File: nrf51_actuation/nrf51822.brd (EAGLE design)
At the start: 40 x 27.8 mm, 22 parts, among them T1 MMUN2238

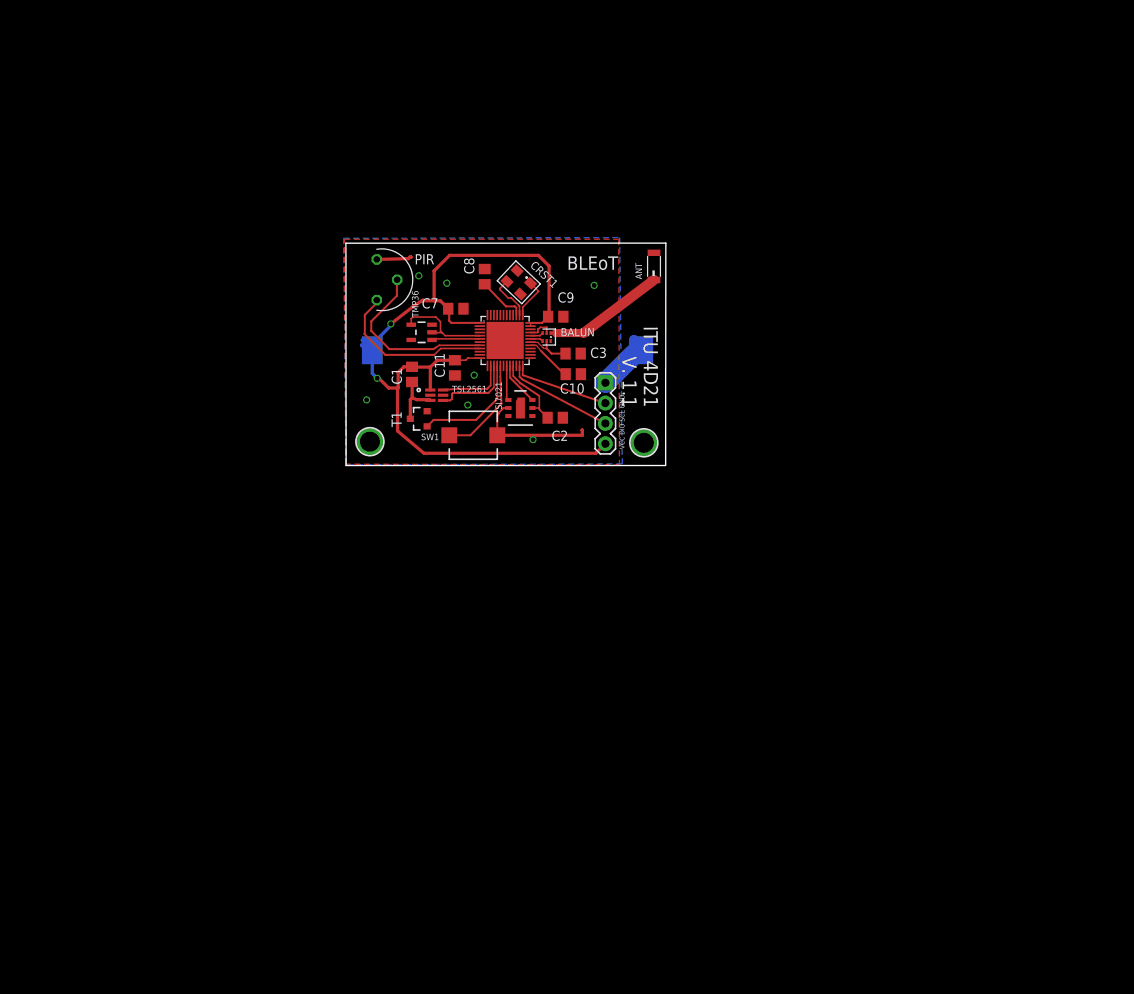
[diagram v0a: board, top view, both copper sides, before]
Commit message: Sensor board should be 100% done... Waiting for boards from slow china :0)
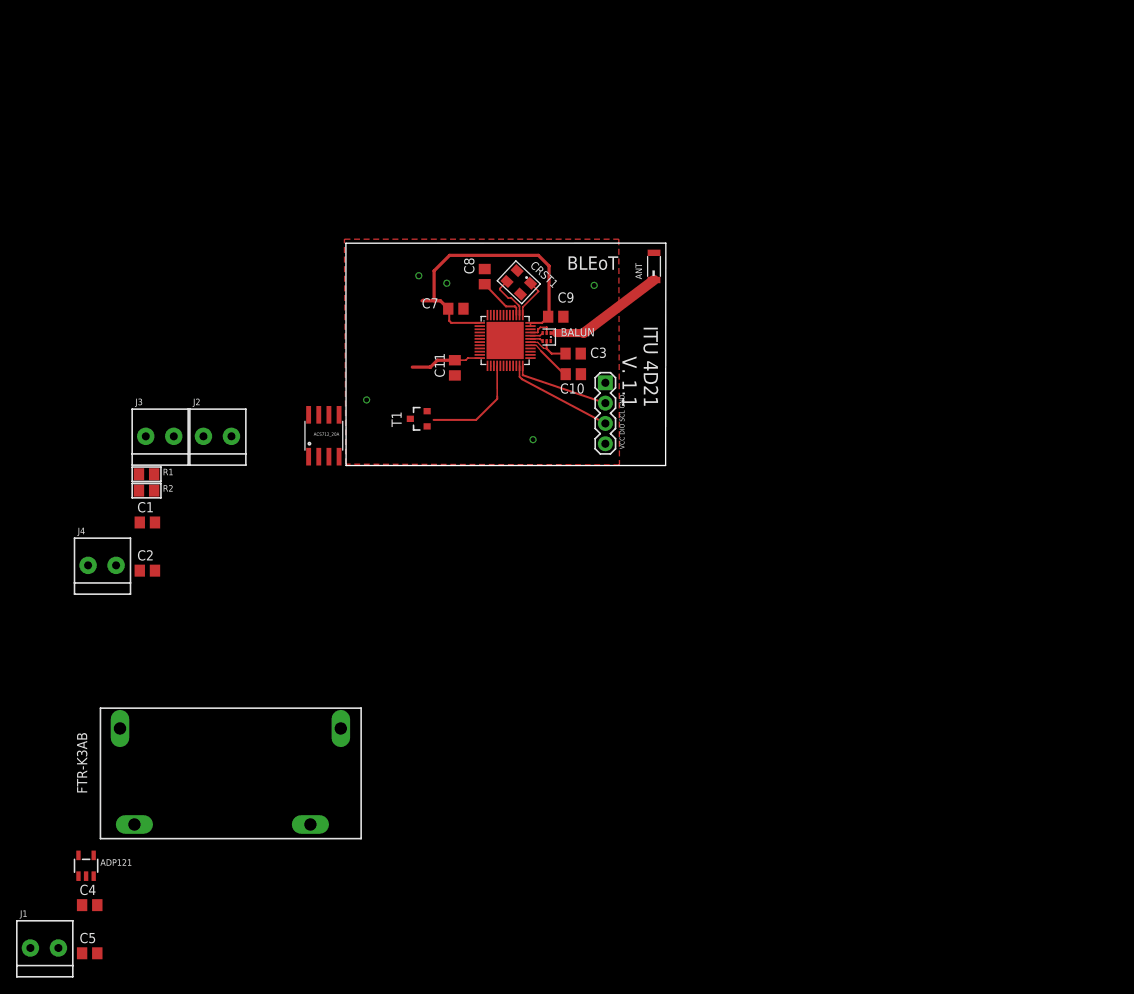
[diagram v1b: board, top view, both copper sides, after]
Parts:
- removed CR2450: 3.3V, NordicSemi:CR2450
- removed PIR: EKMB1303112, NordicSemi:TO5
- removed SI7021: SI7021SMD, NordicSemi:SI7021
- removed SW1: (no value), microbuilder:PUSHBUTTON_SMD_SJ
- removed TMP36: TMP36_SOT23_5, NordicSemi:SOT23-5
- removed TSL2561: LIGHT_TSL2561, microbuilder:TSL2561_FN
- removed U$6, U$7: MOUNTINGHOLE2.5, microbuilder:MOUNTINGHOLE_2.5_PLATED
- added ACS712_20A: ACS712, SparkFun-AnalogIC:SO08
- added ADP121: (no value), microbuilder:SOT23-5
- added C4, C5: 10uF, rcl:C0805
- added FTR-K3AB: FTR-K3AB, NordicSemi:FTR-K1C
- added J1, J2, J3, J4: (no value), microbuilder:TERMBLOCK_1X2-3.5MM
- added R1, R2: (no value), microbuilder:0805
- C1: value 100nF -> 1nF
- moved C2 54.4 mm to (-23.3, -11.3)
- moved C1 37.9 mm to (-23.3, -5.31), turned to 0 degrees
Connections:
- removed net GIOP3: SW1.P$2, U$4.17
- new net 5.0V: ACS712_20A.8, ADP121.1, ADP121.3, C2.1, C5.1, FTR-K3AB.1, J3.1
- new net N$11: ACS712_20A.6, C1.1
- new net N$15: ACS712_20A.7, R1.1
- new net ROUT1: ACS712_20A.1, ACS712_20A.2, FTR-K3AB.4, J2.1, J4.1
- new net ROUT2: ACS712_20A.3, ACS712_20A.4, FTR-K3AB.3, J2.2, J4.2
- new net TERMO1: J1.1
- new net TERMO2: J1.2
- net AIN0/XL2: now also R1.2, R2.1
- net AIN2: no longer TMP36.2, TMP36.4
- net AIN3: no longer TMP36.1
- net AIN5: no longer PIR.2
- net AIN6: no longer PIR.1
- net GIOP0: no longer TSL2561.DATA
- net GIOP1: no longer TSL2561.CLK
- net GIOP5: no longer SI7021.1
- net GIOP6: no longer SI7021.6
- net GIOP7: no longer C2.1, SI7021.5
- net GND: now also ACS712_20A.5, ADP121.2, C1.2, C4.2, C5.2, J3.2, R2.2; no longer CR2450.NEG, PIR.3, SI7021.2, SW1.P$1, TMP36.5
- net N$7: now also FTR-K3AB.2; no longer C1.1, TSL2561.VSS
- net VDD: now also ADP121.5, C4.1; no longer C1.2, CR2450.POS, TSL2561.VDD
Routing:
- net VDD: track 108.3 -> 49.5 mm, vias 2 -> 0
- net GND: track 31.9 -> 3.31 mm, vias 7 -> 5
- net AIN5: track 22.4 -> 0.00 mm
- net AIN6: track 20.7 -> 0.00 mm
- net GIOP3: track 12.9 -> 0.00 mm
- net AIN2: track 12.4 -> 0.01 mm
- net GIOP1: track 10.1 -> 0.00 mm
- net GIOP7: track 9.43 -> 0.00 mm
- net GIOP0: track 8.61 -> 0.04 mm
- net N$7: track 7.19 -> 0.00 mm
- net AIN3: track 6.02 -> 0.00 mm
- net GIOP6: track 5.43 -> 0.00 mm
- net GIOP5: track 4.36 -> 0.00 mm
- net GIOP2: track 14.4 -> 13.2 mm
- removed copper zone on layer 16, net GND

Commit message: Done with routing.. should be more or less done
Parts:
- removed J3: (no value), microbuilder:TERMBLOCK_1X2-3.5MM
- added AD8495: AD8495, NordicSemi:MSOP-8
- added C12: 100nF, rcl:C0805
- added C13, C14: 12pF, rcl:C0805
- added C6: 10nF, rcl:C0805
- added FB1, FB2: (no value), microbuilder:0805
- added IRM-05-5: IRM05-5V, NordicSemi:IRM05
- added U$1, U$13, U$14, U$7: MOUNTINGHOLE2.5, microbuilder:MOUNTINGHOLE_2.5_PLATED
- moved FTR-K3AB 124.4 mm to (79.7, 45.7)
- moved J4 123.7 mm to (93.8, 3.89), turned to 180 degrees
- moved C5 111.2 mm to (48.6, 18.9), turned to 270 degrees
- moved C4 102.3 mm to (41.5, 19.5), turned to 90 degrees
- moved ADP121 101.8 mm to (45.0, 19.5), turned to 90 degrees
- moved J1 81.7 mm to (4.34, 12.4), turned to 90 degrees
- moved C2 71.9 mm to (24.4, 42.4), turned to 270 degrees
- moved C1 65.0 mm to (19.3, 43.7), turned to 180 degrees
- moved R1 55.7 mm to (22.5, 32.2), turned to 270 degrees
- moved R2 52.8 mm to (22.6, 24.6), turned to 211.8 degrees
- moved J2 51.1 mm to (4.36, 52.9), turned to 90 degrees
- moved ACS712_20A 49.0 mm to (21.9, 48.7), turned to 180 degrees
- moved T1 39.7 mm to (50.3, 7.29), turned to 270 degrees
- moved ANT 25.8 mm to (46.6, 1.81), turned to 0 degrees
- moved C8 9.69 mm to (27.2, 20.5), turned to 0 degrees
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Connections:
- removed net ROUT1: ACS712_20A.1, ACS712_20A.2, FTR-K3AB.4, J2.1, J4.1
- removed net ROUT2: ACS712_20A.3, ACS712_20A.4, FTR-K3AB.3, J2.2, J4.2
- removed net TERMO1: J1.1
- removed net TERMO2: J1.2
- new net AC/L: ACS712_20A.1, ACS712_20A.2, IRM-05-5.AC/L, J4.1
- new net AC/LOUT: ACS712_20A.3, ACS712_20A.4, J2.2
- new net AC/N: FTR-K3AB.3, IRM-05-5.AC/N, J4.2
- new net AC/NOUT: FTR-K3AB.4, J2.1
- new net GIOP10: U$4.25
- new net GIOP3: U$4.17
- new net N$16: AD8495.1, C6.2, FB2.2
- new net N$17: FB2.1, J1.2
- new net N$8: FB1.1, J1.1
- new net N$9: AD8495.8, C6.1, FB1.2
- net 5.0V: now also AD8495.7, C12.2, IRM-05-5.+V; no longer J3.1
- net AIN4: now also AD8495.5, AD8495.6
- net GND: now also AD8495.2, AD8495.3, C12.1, C13.1, C14.1, IRM-05-5.-V; no longer J3.2
- net N$1: now also C14.2, CRST1.H2, U$4.38; no longer CRST1.H1, U$4.37
- net N$2: now also C13.2, CRST1.H1, U$4.37; no longer CRST1.H2, U$4.38
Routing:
- net 5.0V: track 0.00 -> 152.5 mm, vias 0 -> 2
- net AC/L: track 0.00 -> 98.1 mm, vias 0 -> 1
- net AC/NOUT: track 0.00 -> 63.2 mm
- net N$7: track 0.00 -> 53.8 mm
- net AC/N: track 0.00 -> 50.0 mm
- net VDD: track 49.5 -> 96.4 mm, vias 0 -> 4
- net GND: track 3.31 -> 26.7 mm, vias 5 -> 9
- net AC/LOUT: track 0.00 -> 18.2 mm
- net GIOP2: track 13.2 -> 29.8 mm, vias 0 -> 3
- net AIN0/XL2: track 0.00 -> 16.2 mm
- net N$15: track 0.00 -> 12.9 mm
- net AIN4: track 0.00 -> 8.01 mm
- net N$16: track 0.00 -> 7.39 mm
- net N$9: track 0.00 -> 6.45 mm
- net N$3: track 15.1 -> 21.4 mm
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- added copper zone on layer 16, net GND
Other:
- board size 40 x 27.8 mm -> 97.2 x 56.6 mm
- board text removed: "BLEoT"
- board text removed: "ITU 4D21 V. 1.1"
- board text removed: "VCC DIO SCL GND"

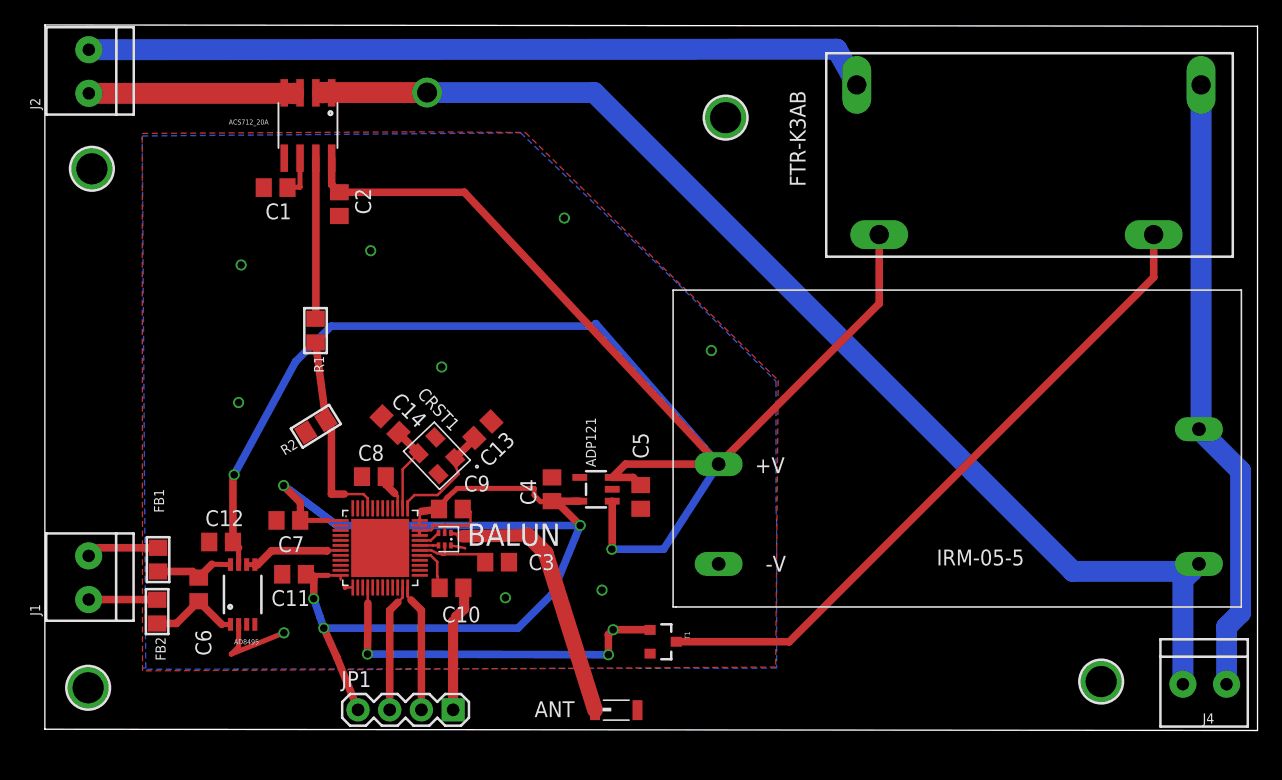
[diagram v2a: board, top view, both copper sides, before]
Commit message: CLEANED AND ADDED COMMENTS / TAGS ACTUATION MADE 45% SMALLER
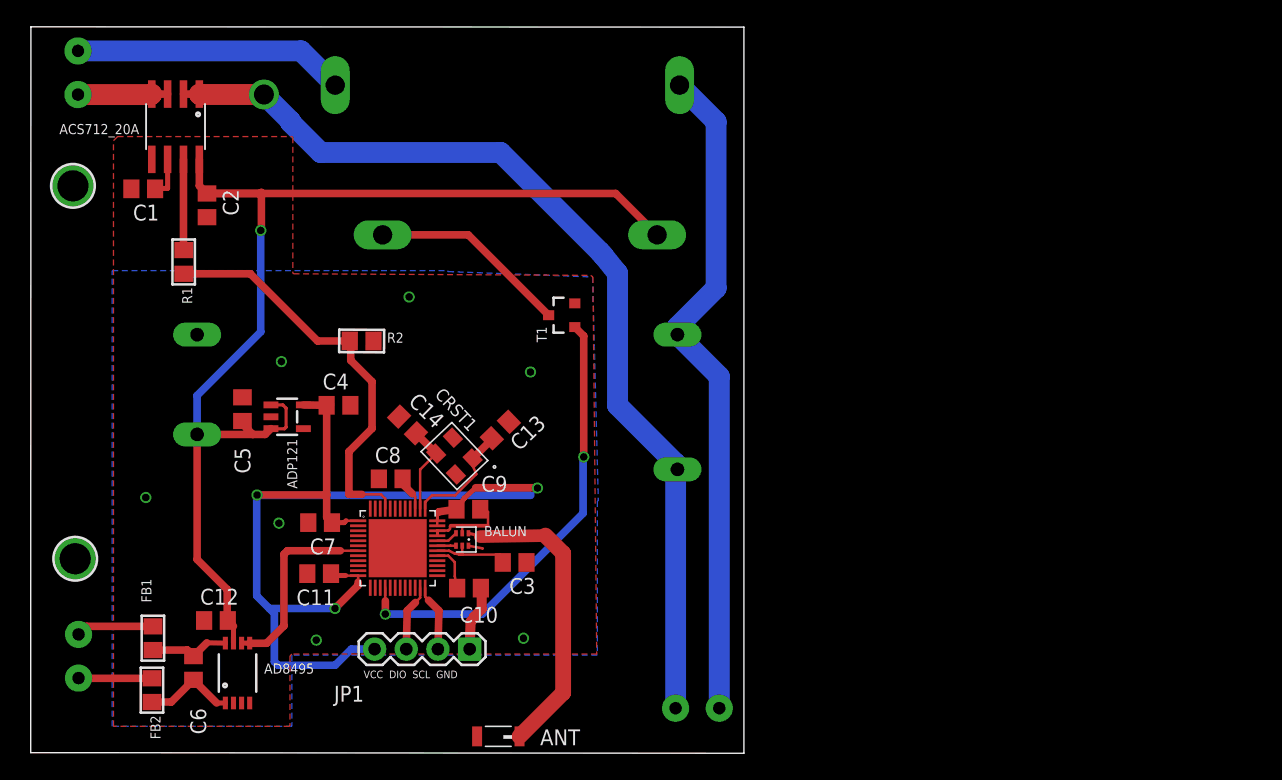
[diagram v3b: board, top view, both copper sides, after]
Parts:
- removed U$13, U$14: MOUNTINGHOLE2.5, microbuilder:MOUNTINGHOLE_2.5_PLATED
- R1: value (none) -> 2k
- R2: value (none) -> 8k
- moved IRM-05-5 41.9 mm to (51.5, 21.2), flipped to the bottom, turned to 0 degrees
- moved FTR-K3AB 41.8 mm to (37.9, 45.7), flipped to the bottom
- moved J4 40.8 mm to (53.1, 1.97), flipped to the bottom
- moved C5 32.7 mm to (16.7, 25.9), turned to 90 degrees
- moved T1 27.4 mm to (42.3, 33.5), turned to 90 degrees
- moved ADP121 25.4 mm to (20.3, 25.3), turned to 270 degrees
- moved C4 18.4 mm to (24.4, 26.2), turned to 0 degrees
- moved R1 11.9 mm to (12.0, 37.7)
- moved C1 10.6 mm to (8.72, 43.6)
- moved ACS712_20A 10.6 mm to (11.3, 48.6)
- moved C2 10.6 mm to (13.8, 42.3)
- moved U$1 10.4 mm to (3.26, 13.9)
- moved ANT 9.69 mm to (37.2, -0.29), turned to 180 degrees
- moved R2 7.76 mm to (26.2, 31.4), turned to 359.7 degrees
- moved J1 6.35 mm to (3.53, 6.08), flipped to the bottom
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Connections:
- net AC/L: now also FTR-K3AB.4; no longer ACS712_20A.1, ACS712_20A.2
- net AC/LOUT: now also FTR-K3AB.3, J2.1; no longer ACS712_20A.3, ACS712_20A.4, J2.2
- net AC/N: now also ACS712_20A.1, ACS712_20A.2; no longer FTR-K3AB.3
- net AC/NOUT: now also ACS712_20A.3, ACS712_20A.4, J2.2; no longer FTR-K3AB.4, J2.1
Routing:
- net 5.0V: track 152.5 -> 96.0 mm, vias 2 -> 1
- net AC/NOUT: track 63.2 -> 7.20 mm
- net AC/L: track 98.1 -> 53.8 mm, vias 1 -> 0
- net N$7: track 53.8 -> 16.0 mm
- net AC/N: track 50.0 -> 77.9 mm, vias 0 -> 1
- net AIN0/XL2: track 16.2 -> 33.2 mm
- net GND: track 26.7 -> 14.1 mm, vias 9 -> 7
- net AIN4: track 8.01 -> 15.8 mm
- net GIOP2: track 29.8 -> 36.6 mm, vias 3 -> 2
- net VDD: track 96.4 -> 90.5 mm, vias 4 -> 3
- net N$15: track 12.9 -> 7.28 mm
- net N$14: track 10.3 -> 5.37 mm
- net N$12: track 10.2 -> 5.35 mm
- net AC/LOUT: track 18.2 -> 21.8 mm
- net N$3: track 21.4 -> 24.3 mm
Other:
- board size 97.2 x 56.6 mm -> 57.2 x 58.2 mm
- board text added: "VCC DIO SCL GND"

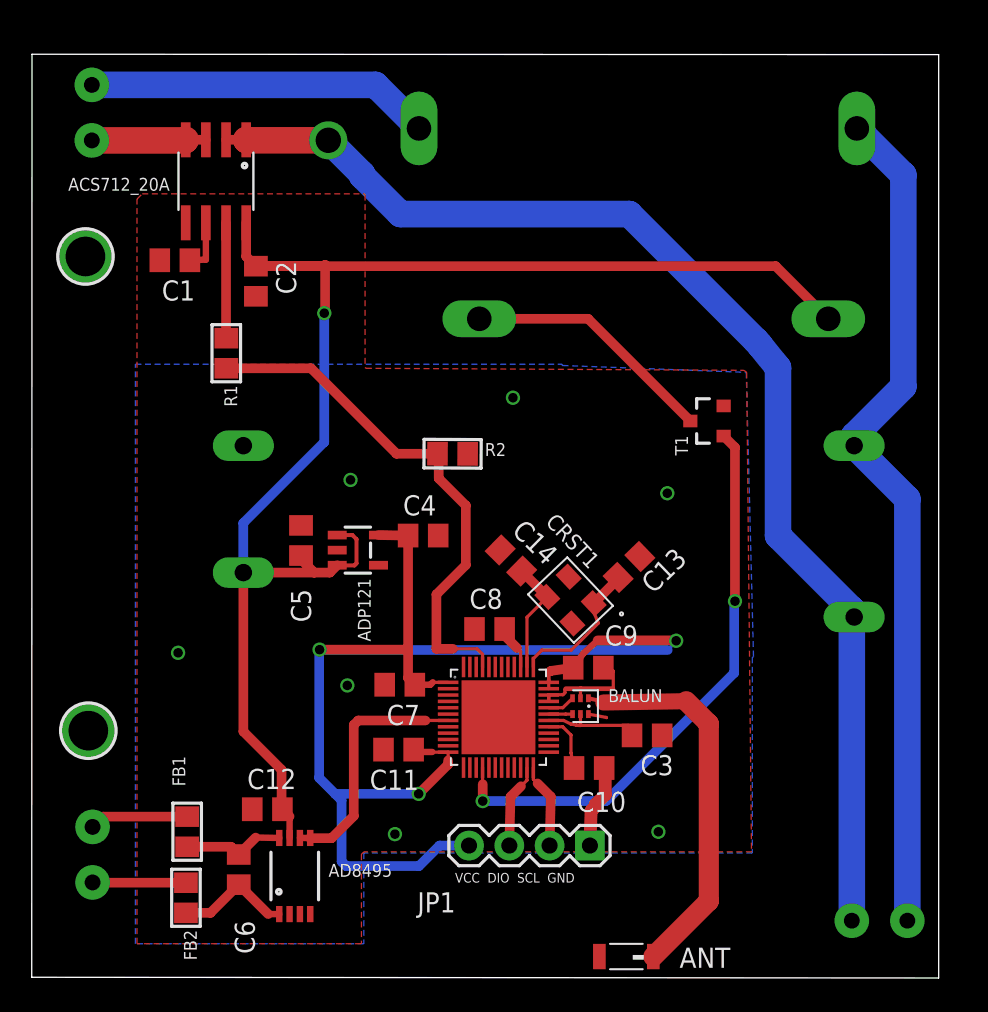
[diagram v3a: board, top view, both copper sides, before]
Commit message: Added optional low pass filter circut and cleaned up some more
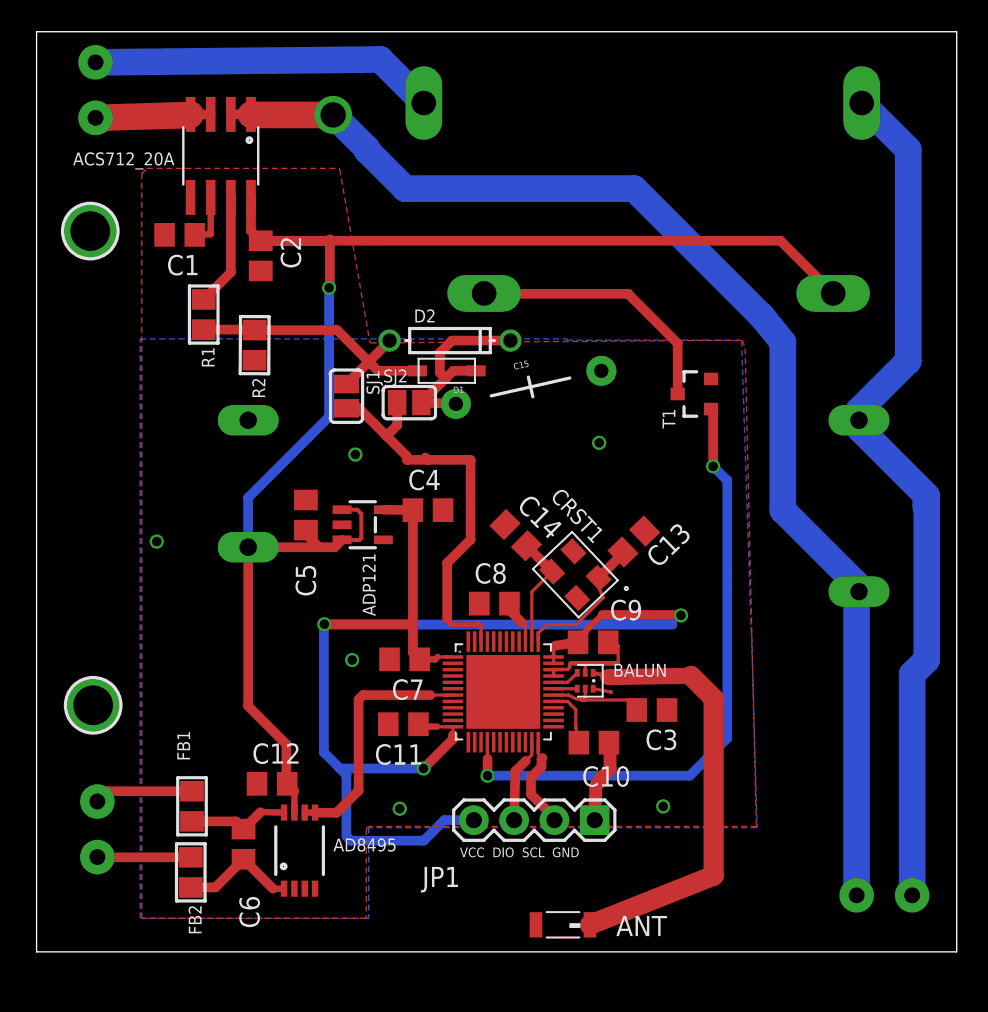
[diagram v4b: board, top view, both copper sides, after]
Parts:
- added C15: (no value), SparkFun-Capacitors:CAP-PTH-LARGE
- added D1: (no value), adafruit:SOD-123
- added D2: (no value), microbuilder:DO-1N4148
- added SJ1, SJ2: SOLDERJUMPERREFLOW_NOPASTE, microbuilder:SOLDERJUMPER_REFLOW_NOPASTE
- moved R2 14.2 mm to (13.7, 38.2), turned to 269.7 degrees
- moved ANT 4.47 mm to (33.2, 1.71)
- moved R1 2.82 mm to (10.5, 40.2)
- moved T1 1.88 mm to (41.5, 35.2)
- moved ACS712_20A 1.63 mm to (11.6, 50.2)
- moved ADP121 1.63 mm to (20.6, 26.9)
- moved C1 1.63 mm to (9.02, 45.2)
- moved C10 1.63 mm to (35.1, 13.2)
- moved C14 1.63 mm to (30.2, 26.3)
- moved C2 1.63 mm to (14.1, 43.9)
- moved C3 1.63 mm to (38.8, 15.2)
- moved C4 1.63 mm to (24.7, 27.8)
- moved C5 1.63 mm to (17.0, 27.5)
- moved C7 1.63 mm to (23.2, 18.4)
- moved C9 1.63 mm to (35.1, 19.5)
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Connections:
- new net N$15: D1.A, D2.A, R1.2, R2.1, SJ1.1
- new net N$19: C15.1, D1.C, D2.C, SJ2.2
- net AIN0/XL2: no longer R1.2, R2.1
- net AIN1/XL1: now also SJ1.2, SJ2.1
- net GND: now also C15.2
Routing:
- net AIN0/XL2: track 33.2 -> 0.00 mm
- net AIN1/XL1: track 0.00 -> 25.9 mm
- net N$15: track 0.00 -> 18.5 mm
- net N$19: track 0.00 -> 13.3 mm
- net N$3: track 24.3 -> 27.8 mm
- net GIOP2: track 36.6 -> 39.4 mm
- net AC/L: track 53.8 -> 55.9 mm
- net N$7: track 16.0 -> 16.7 mm
- net N$14: track 5.37 -> 5.95 mm
- net GND: vias 7 -> 6
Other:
- board size 57.2 x 58.2 mm -> 58 x 58 mm
